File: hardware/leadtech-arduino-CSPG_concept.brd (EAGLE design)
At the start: 100 x 80 mm, 51 parts, among them IC1 CD4050B, IC2 LM358D, J1 CON_HEADER_1X08-PTH, J2 CON_HEADER_1X08-PTH, J3 CON_HEADER_1X08-PTH, J4 CON_HEADER_1X06-PTH, J5 CON_HEADER_1X05-PTH, J6 CON_HEADER_1X02-PTH, J7 CON_HEADER_1X05-PTH, J8 CON_HEADER_1X08-PTH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

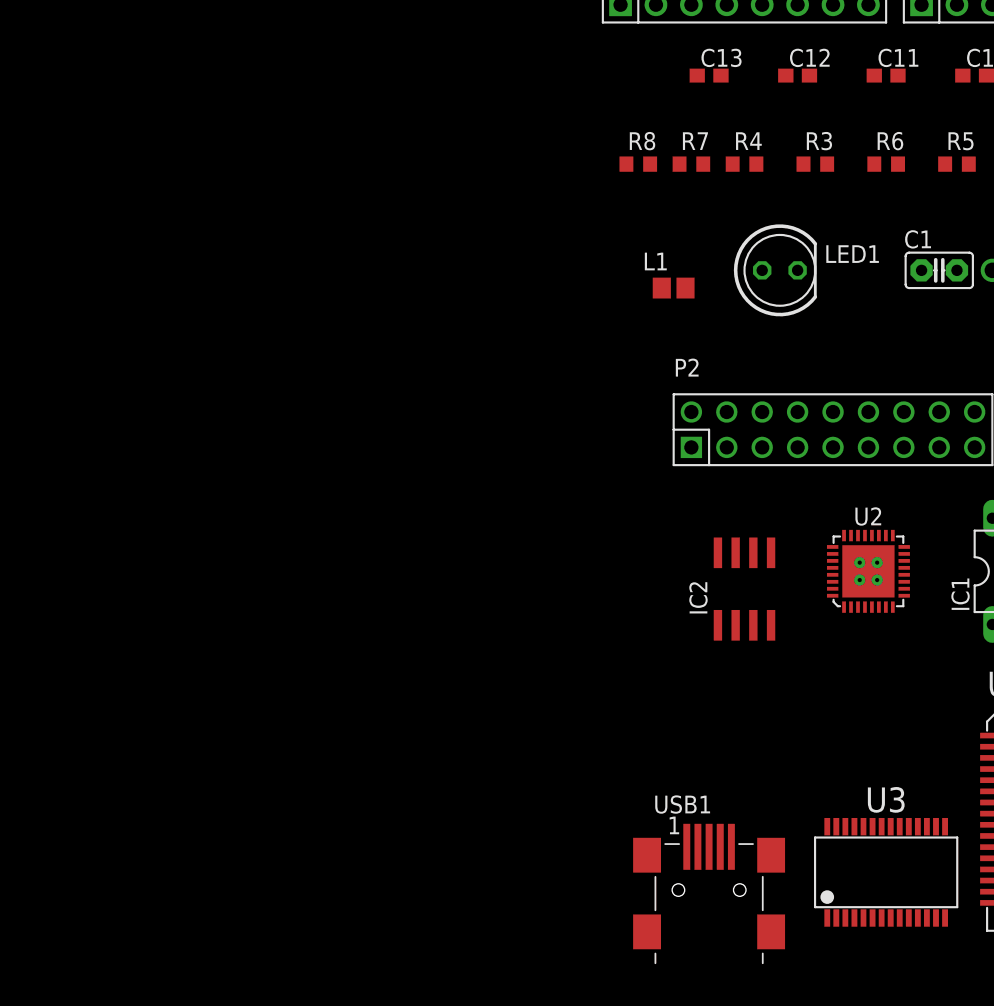
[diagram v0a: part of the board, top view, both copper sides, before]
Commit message: add project schedule excel, add RFID module on schematic
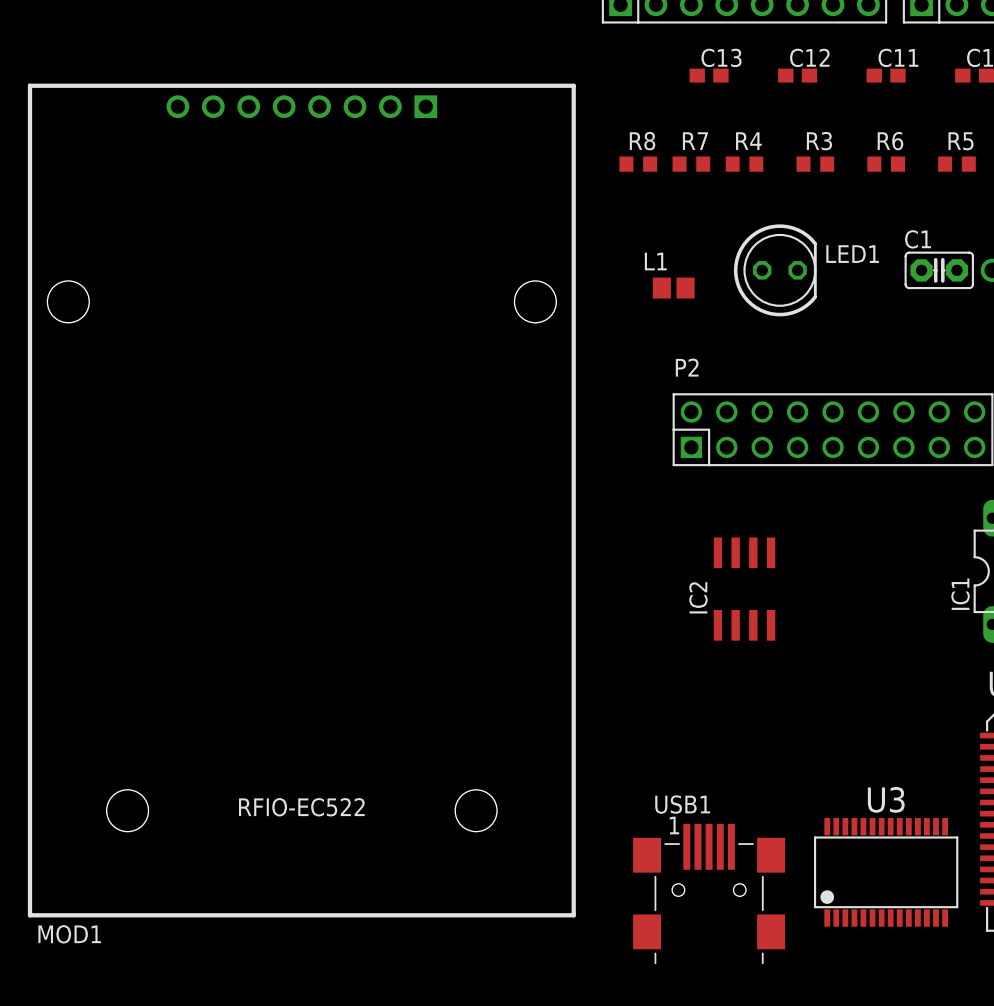
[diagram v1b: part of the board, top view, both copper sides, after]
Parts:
- removed U2: MFRC522, trosh_devices.eagle.v9:HVQFN-32
- added MOD1: RFIO-RC522, trosh_devices.eagle.v9:RFIO-RC522
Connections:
- removed net AVDD: U2.P15
- removed net AVSS: U2.P18
- removed net DVDD: U2.P3
- removed net DVSS: U2.P4
- removed net PVDD: U2.P2
- removed net PVSS: U2.P5
- removed net SVDD: U2.P9
- removed net TVDD: U2.P12
- removed net TVSS: U2.P10, U2.P14
- removed net VMID: U2.P16
- net GND: now also MOD1.P6
- net N$1: now also MOD1.P8; no longer J8.8
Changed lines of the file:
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@@
 <attribute name="VALUE" x="-17.78" y="25.98" size="1.778" layer="27" font="vector" align="center"/>
-</element>
-<element name="U2" library="trosh_devices.eagle.v9" package="HVQFN-32" value="MFRC522" x="-58.42" y="29.21" smashed="yes">
-<attribute name="NAME" x="-58.42" y="33.147" size="1.27" layer="25" font="vector" align="center"/>
-<attribute name="VALUE" x="-58.42" y="25.273" size="1.27" layer="27" font="vector" align="center"/>
 </element>
 <element name="U3" library="trosh_devices.eagle.v9" package="SSOP-28" value="PL2303HX" x="-57.15" y="7.62" smashed="yes">
@@
 <attribute name="NAME" x="-30.48" y="59.69" size="1.27" layer="25" font="vector" ratio="10"/>
 <attribute name="VALUE" x="-30.48" y="55.88" size="1.27" layer="27" font="vector" ratio="10"/>
+</element>
+<element name="MOD1" library="trosh_devices.eagle.v9" package="RFIO-RC522" value="RFIO-RC522" x="-99.06" y="34.29" smashed="yes">
+<attribute name="NAME" x="-118.11" y="2.54" size="1.27" layer="25" font="vector" ratio="12"/>
+<attribute name="VALUE" x="-118.11" y="1.27" size="1.27" layer="27" font="vector" ratio="12"/>
 </element>
 </elements>
@@
 <signal name="V-">
 <contactref element="IC2" pad="4"/>
-</signal>
-<signal name="PVDD">
-<contactref element="U2" pad="P2"/>
-</signal>
-<signal name="DVDD">
-<contactref element="U2" pad="P3"/>
-</signal>
-<signal name="DVSS">
-<contactref element="U2" pad="P4"/>
-</signal>
-<signal name="PVSS">
-<contactref element="U2" pad="P5"/>
-</signal>
-<signal name="SVDD">
-<contactref element="U2" pad="P9"/>
-</signal>
-<signal name="TVSS">
-<contactref element="U2" pad="P10"/>
-<contactref element="U2" pad="P14"/>
-<wire x1="-57.67" y1="31.775" x2="-59.67" y2="31.775" width="0" layer="19" extent="1-1"/>
-</signal>
-<signal name="TVDD">
-<contactref element="U2" pad="P12"/>
-</signal>
-<signal name="AVDD">
-<contactref element="U2" pad="P15"/>
-</signal>
-<signal name="VMID">
-<contactref element="U2" pad="P16"/>
-</signal>
-<signal name="AVSS">
-<contactref element="U2" pad="P18"/>
 </signal>
 <signal name="ARDUINO-5">
@@
 <contactref element="C12" pad="2"/>
 <contactref element="C11" pad="2"/>
+<contactref element="MOD1" pad="P6"/>
 <wire x1="-20.32" y1="74.93" x2="-15.24" y2="80.01" width="0" layer="19" extent="1-1"/>
 <wire x1="-24.13" y1="80.01" x2="-20.32" y2="74.93" width="0" layer="19" extent="1-1"/>
@@
 <wire x1="-43.91" y1="3.68" x2="-54.875" y2="10.895" width="0" layer="19" extent="1-1"/>
 <wire x1="-22.86" y1="3.175" x2="-43.91" y2="3.68" width="0" layer="19" extent="1-1"/>
+<wire x1="-102.87" y1="62.54" x2="-74.93" y2="74.93" width="0" layer="19" extent="1-1"/>
 </signal>
 <signal name="+5V">
@@
 <contactref element="ZD1" pad="C"/>
 <contactref element="R5" pad="2"/>
-<contactref element="J8" pad="8"/>
 <contactref element="IC1" pad="1"/>
 <contactref element="C1" pad="1"/>
-<wire x1="-30.845" y1="58.42" x2="-15.24" y2="74.93" width="0" layer="19" extent="1-1"/>
-<wire x1="-51.22" y1="58.42" x2="-30.845" y2="58.42" width="0" layer="19" extent="1-1"/>
-<wire x1="-54.61" y1="50.8" x2="-51.22" y2="58.42" width="0" layer="19" extent="1-1"/>
+<contactref element="MOD1" pad="P8"/>
+<wire x1="-54.61" y1="50.8" x2="-107.95" y2="62.54" width="0" layer="19" extent="1-1"/>
+<wire x1="-51.22" y1="58.42" x2="-54.61" y2="50.8" width="0" layer="19" extent="1-1"/>
+<wire x1="-30.845" y1="58.42" x2="-51.22" y2="58.42" width="0" layer="19" extent="1-1"/>
 <wire x1="-49.53" y1="25.4" x2="-54.61" y2="50.8" width="0" layer="19" extent="1-1"/>
 </signal>

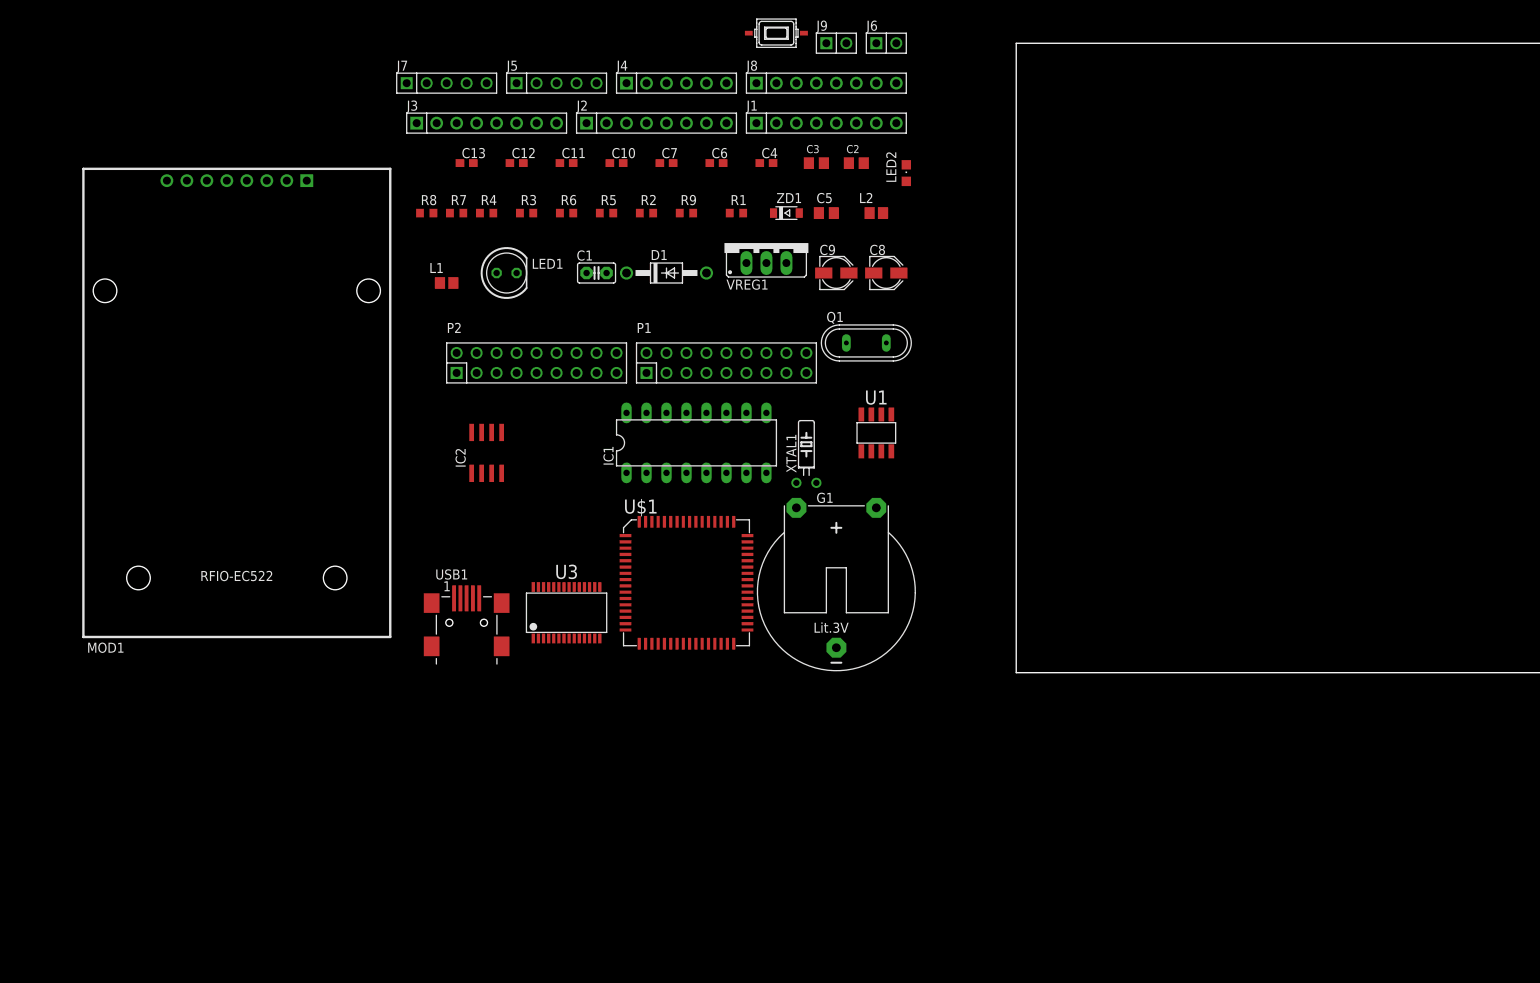
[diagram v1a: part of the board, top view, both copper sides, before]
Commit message: continue wiring schematic, RFIF wiring done, level shifter done, add BOM with links on excel sheet
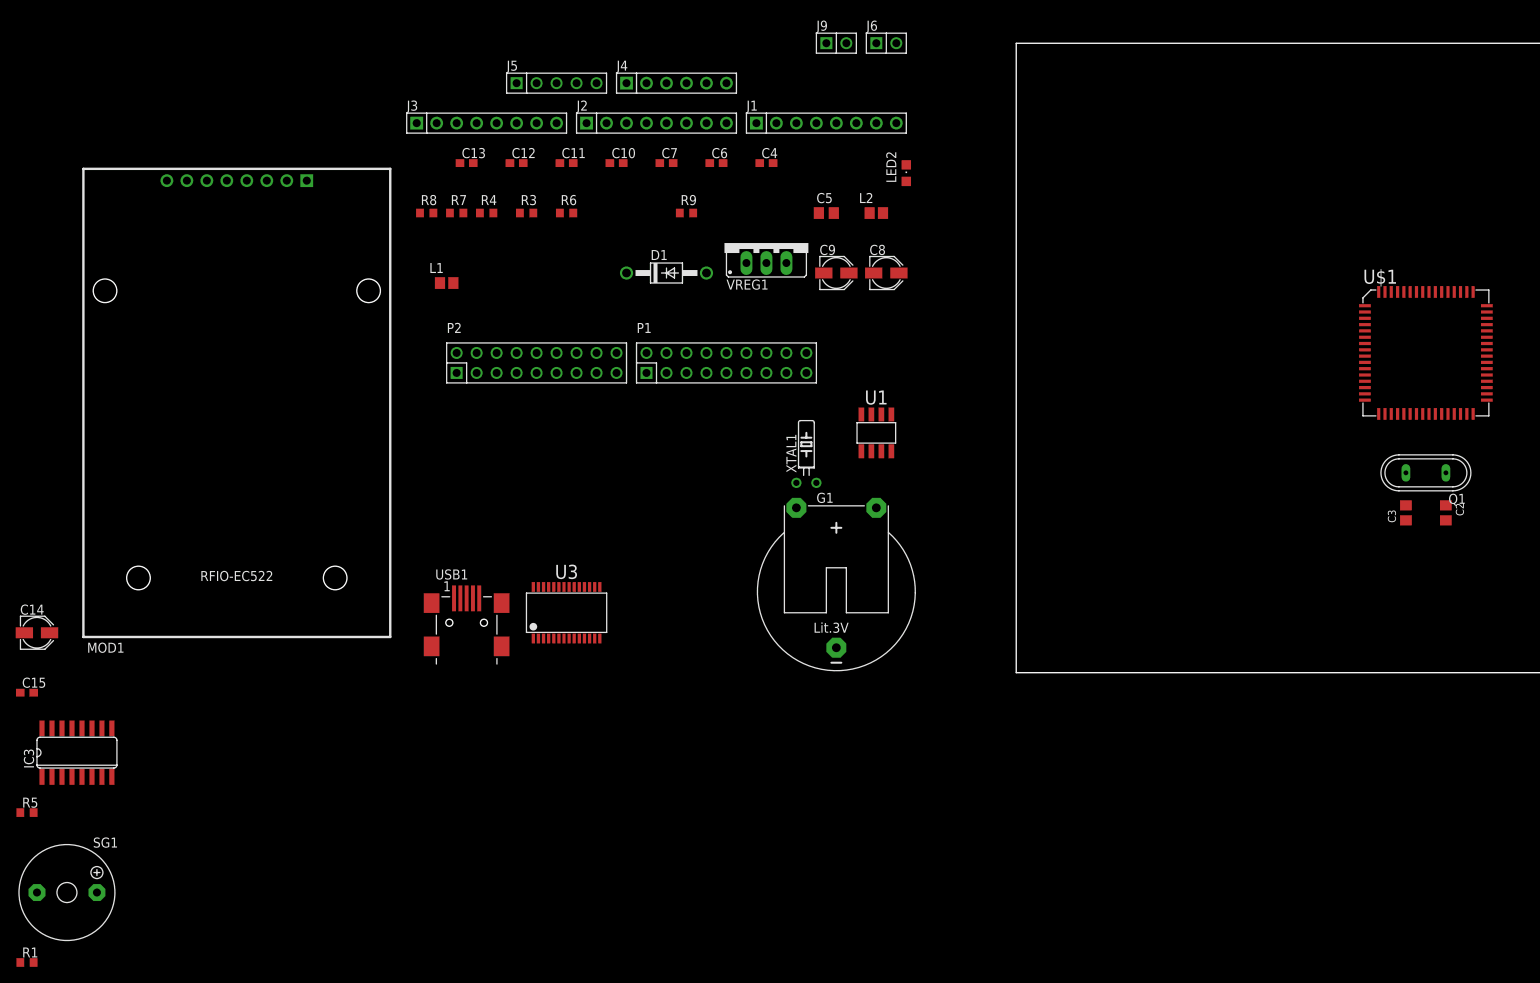
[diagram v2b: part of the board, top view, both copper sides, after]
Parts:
- removed C1: 0.1uF, dp_devices.v6:C0.1PTH
- removed IC1: CD4050B, 40xx:DIL16
- removed IC2: LM358D, linear:SO08
- removed J7: CON_HEADER_1X05-PTH, dp_devices.v6:M1X5
- removed J8: CON_HEADER_1X08-PTH, dp_devices.v6:M1X8
- removed LED1: (no value), dp_devices.v6:LED-5MM
- removed R2: 4.7K, dp_devices.v6:R603
- removed SW1: SW_TACT_2P-3X6, dp_devices.v6:SW_TACT_3X6
- removed ZD1: 3.3V, dp_devices.v6:SOD-123
- added C14: 100uF, dp_devices.v6:CASE_B
- added C15: 0.1uF, rcl:C0603
- added IC3: 4050D, 40xx:SO16
- added SG1: F/TMB, buzzer:F/TMB
- R1: value 330R -> 10K; device dp_devices.v6:R603 -> rcl:R0603
- R5: value 4.7K -> 10K; device dp_devices.v6:R603 -> rcl:R0603
- moved R1 131.2 mm to (-125.7, -36.8)
- moved R5 106.0 mm to (-125.7, -17.8)
- moved U$1 98.4 mm to (52.1, 40.6)
- moved C2 87.1 mm to (54.6, 20.3), turned to 270 degrees
- moved C3 87.1 mm to (49.5, 20.3), turned to 90 degrees
- moved Q1 73.0 mm to (52.1, 25.4), turned to 180 degrees
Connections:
- removed net ARDUINO-10: IC1.3, J1.3
- removed net ARDUINO-12: J1.5, J8.4
- removed net ARDUINO-2: J2.3, R2.2, SW1.1
- removed net ARDUINO-3: J2.4, R1.1
- removed net ARDUINO-5: J2.6, J7.5
- removed net ARDUINO-6: J2.7, J7.4
- removed net ARDUINO-7: J2.8, J7.3
- removed net ARDUINO-9: IC1.9, J1.2
- removed net N$2: IC1.2, J8.1
- removed net N$3: IC1.5, J1.6
- removed net N$4: IC1.4, J8.2
- removed net N$5: IC1.7, J1.4
- removed net N$6: IC1.6, J8.3
- removed net N$7: IC1.10, J8.7
- removed net N$9: LED1.A, R1.2
- removed net V+: IC2.8
- removed net V-: IC2.4
- new net +3V3: C14.+, C15.2, IC3.1, MOD1.P8
- new net OUT1: U$1.7
- new net PIEZO: R1.1, U$1.1
- new net RFID_CLOCK: IC3.5, U$1.11
- new net RFID_CLOCK_3V: IC3.4, MOD1.P2
- new net RFID_DATA: IC3.3, U$1.10
- new net RFID_DATA_3V: IC3.2, MOD1.P1
- new net RFID_MISO: MOD1.P4, U$1.13
- new net RFID_MOSI: IC3.7, U$1.12
- new net RFID_MOSI_3V: IC3.6, MOD1.P3
- new net RFID_RESET: IC3.9, U$1.15
- new net RFID_RESET_3V: IC3.10, MOD1.P7
- new net SW1: R5.1, U$1.6
- net +5V: now also R5.2; no longer J7.1, LED2.A, R2.1, R5.1
- net GND: now also C14.-, C15.1, IC3.8, SG1.-; no longer C1.2, IC1.8, J7.2, J8.6, LED1.K, SW1.2, ZD1.A
- net N$1: now also R1.2, SG1.+; no longer C1.1, IC1.1, MOD1.P8, R5.2, ZD1.C
